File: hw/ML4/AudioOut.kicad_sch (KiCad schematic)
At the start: 24 parts, among them T1 Transformer_1P_1S, U1 LMV324 (Actually LTV9161), U2 LTV-356T, U4 MCP4725xxx-xCH

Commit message: Updates for ML4
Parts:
- R5, R6: value 10k -> 2.2k
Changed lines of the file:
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@@
 			)
 		)
-		(property "Value" "10k"
+		(property "Value" "2.2k"
 			(at 41.91 57.15 0)
 			(effects
@@
 			)
 		)
-		(property "Value" "10k"
+		(property "Value" "2.2k"
 			(at 52.07 62.23 0)
 			(effects

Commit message: Working on JCSC BOM
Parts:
- R1: LCSC (none) -> C4310
- R2: LCSC (none) -> C17530
- R23, R3: LCSC (none) -> C17477
- R24: LCSC (none) -> C17513
- R25: LCSC (none) -> C17633
- R8: value 200 -> 220

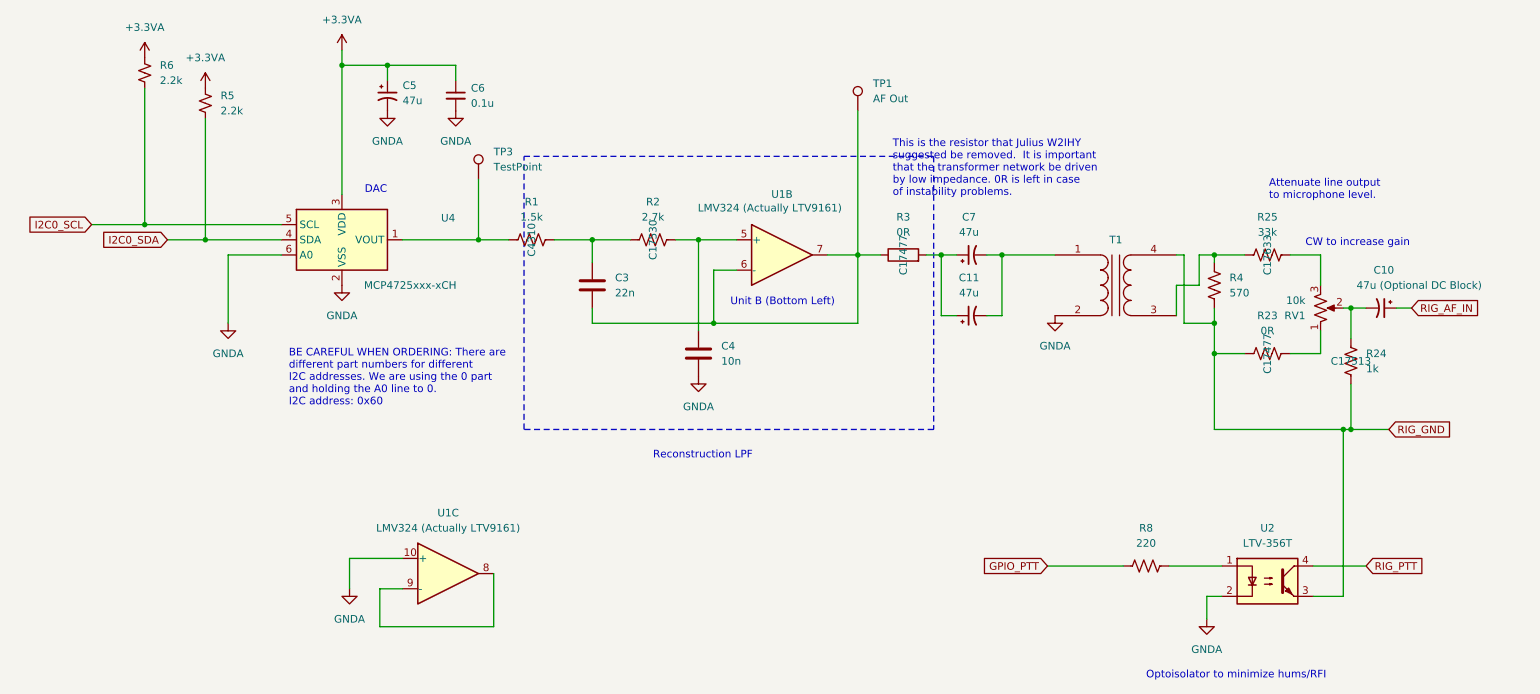
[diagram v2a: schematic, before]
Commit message: Working on adding LCSC part numbers
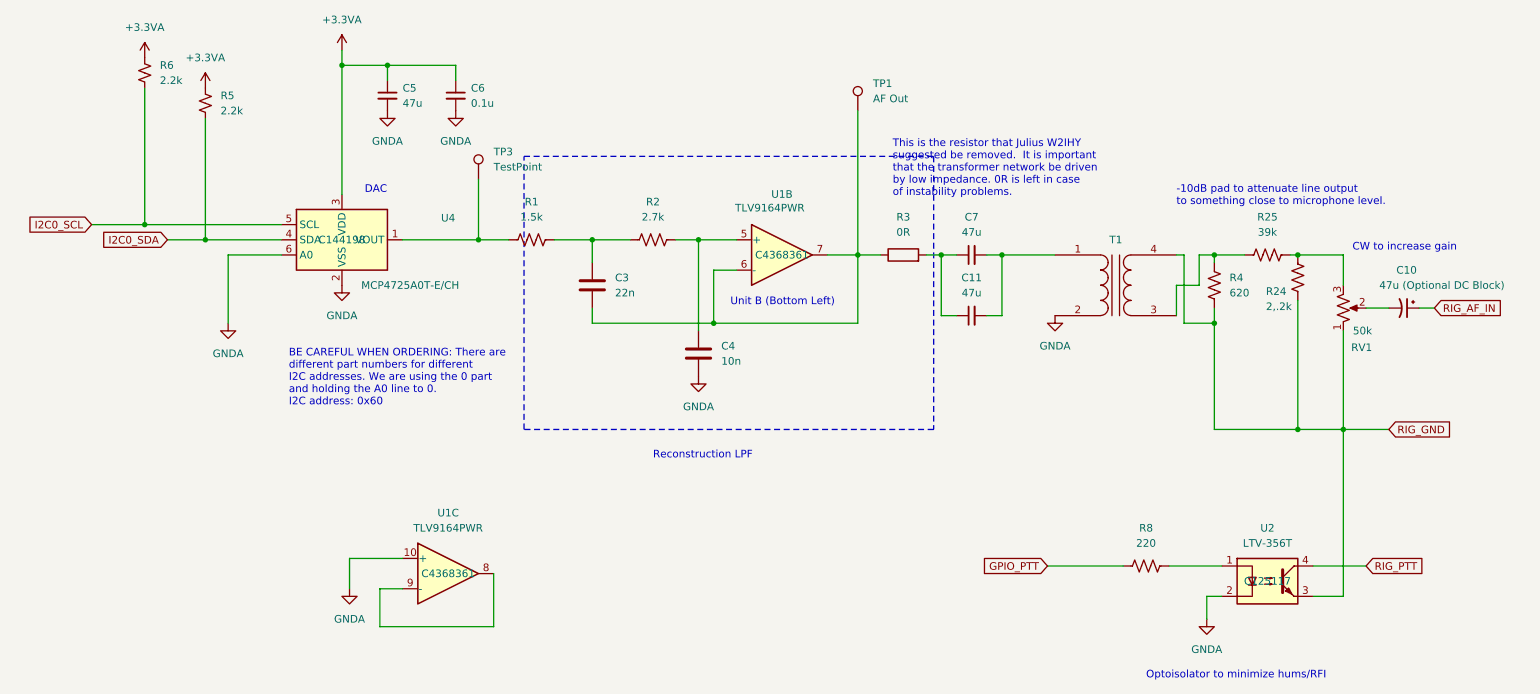
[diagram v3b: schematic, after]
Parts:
- removed C11, C5, C7: 47u, bruce-footprints:CPOL_0805_2012Metric_Pad1.18x1.45mm_HandSolder, symbol Device:C_Polarized_Small_US
- removed R23: 0R, Resistor_SMD:R_0805_2012Metric_Pad1.20x1.40mm_HandSolder, symbol Device:R_US
- added C11, C5, C7: 47u, Capacitor_SMD:C_0805_2012Metric_Pad1.18x1.45mm_HandSolder, symbol Device:C_Small
- C10: LCSC (none) -> C22320
- C3: LCSC (none) -> C1729
- C4: LCSC (none) -> C1710
- C6: LCSC (none) -> C28233
- R24: value 1k -> 2,.2k; LCSC C17513 -> C58595
- R25: value 33k -> 39k; LCSC C17633 -> C58645
- R4: value 570 -> 620; footprint Resistor_SMD:R_0805_2012Metric_Pad1.20x1.40mm_HandSolder -> Resistor_THT:R_Axial_DIN0309_L9.0mm_D3.2mm_P2.54mm_Vertical; LCSC (none) -> C58633
- R5, R6: LCSC (none) -> C17520
- R8: LCSC (none) -> C17557
- RV1: value 10k -> 50k; LCSC (none) -> C81264
- U1: value LMV324 (Actually LTV9161) -> TLV9164PWR; LCSC (none) -> C4368361
- U2: LCSC (none) -> C125117
- U4: value MCP4725xxx-xCH -> MCP4725A0T-E/CH; LCSC (none) -> C144198
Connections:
- net +3.3VA: now also C5.1
- net GNDA: now also C5.2
- net RIG_GND: now also RV1.1
- net at R3.2: now also C11.1, C7.1
- net at T1.1 (AA): now also C11.2, C7.2
- net at C10.2, RV1.2: no longer R24.2
- net at R25.2, RV1.3: now also R24.2
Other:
- note added: "-10dB pad to attenuate line output to something close to microphone level."
- note removed: "Attenuate line output to microphone level."
- moved on the sheet: C10, R24, RV1

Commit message: Working on adding LCSC part numbers
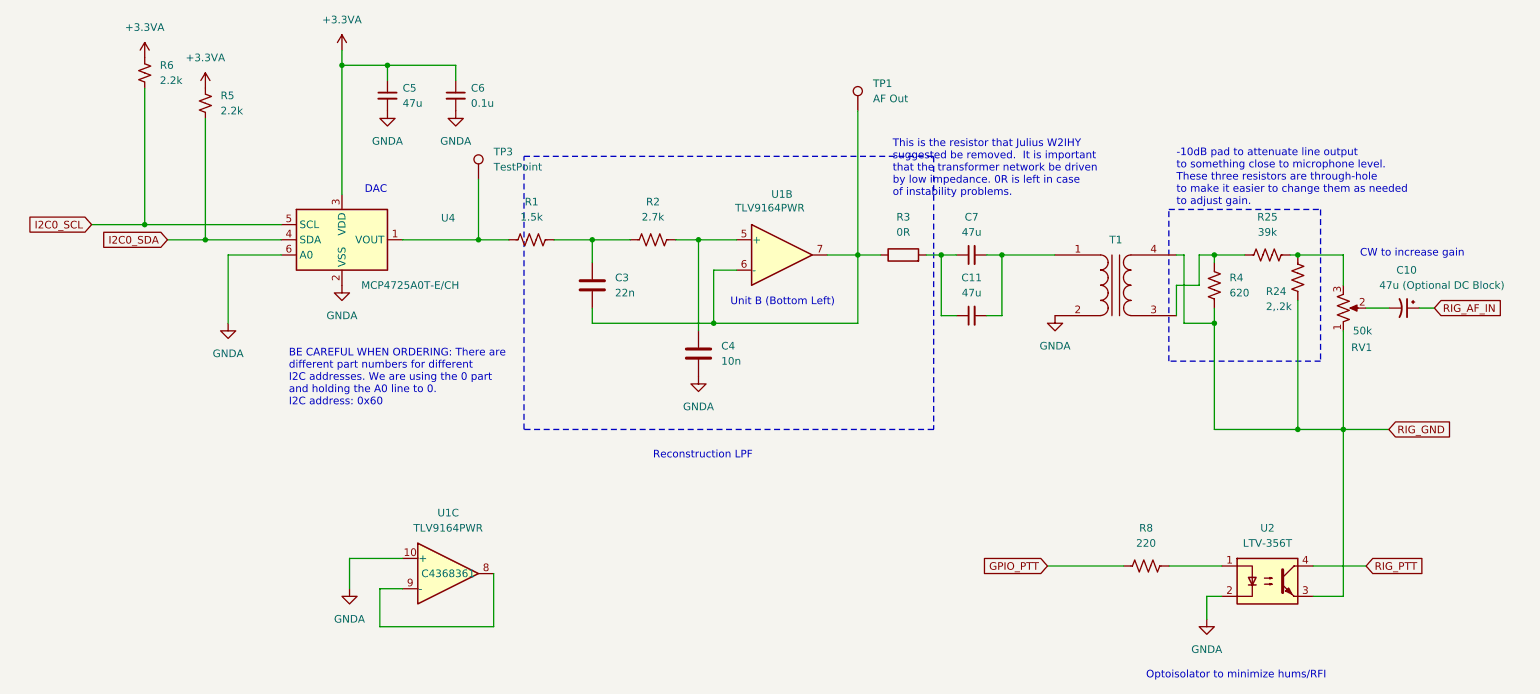
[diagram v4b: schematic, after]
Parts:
- T1: value Transformer_1P_1S -> Transformer_1P_1S 600 Ohm
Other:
- note added: "-10dB pad to attenuate line output to something close to microphone level. These three resistors are through-hole to make it easier to change them as needed to adjust gain."
- note removed: "-10dB pad to attenuate line output to something close to microphone level."
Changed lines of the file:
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@@
 	)
 	(rectangle
+		(start 210.82 78.74)
+		(end 236.22 104.14)
+		(stroke
+			(width 0)
+			(type dot)
+			(color 10 17 255 1)
+		)
+		(fill
+			(type none)
+		)
+	)
+	(rectangle
 		(start 102.87 69.85)
 		(end 171.45 115.57)
@@
 	(text "CW to increase gain"
 		(exclude_from_sim no)
-		(at 241.554 85.852 0)
+		(at 242.824 86.868 0)
 		(effects
 			(font
@@
 		)
 	)
-	(text "-10dB pad to attenuate line output\nto something close to microphone level."
+	(text "-10dB pad to attenuate line output\nto something close to microphone level.\nThese three resistors are through-hole\nto make it easier to change them as needed\nto adjust gain."
 		(exclude_from_sim no)
 		(at 212.09 78.232 0)
@@
 					(size 1.27 1.27)
 				)
+				(hide yes)
 			)
 		)
@@
 					(size 1.27 1.27)
 				)
+				(hide yes)
 			)
 		)
@@
 					(size 1.27 1.27)
 				)
+				(hide yes)
 			)
 		)
@@
 			)
 		)
-		(property "Value" "Transformer_1P_1S"
+		(property "Value" "Transformer_1P_1S 600 Ohm"
 			(at 201.9427 83.82 0)
 			(effects

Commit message: Working on adding LCSC part numbers
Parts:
- T1: BOM Comments (none) -> 600:600 ohm audio transformer (Amazon or AliExpress)
- TP1, TP3: BOM Comments (none) -> No component, PCB test point; now left out of the parts list
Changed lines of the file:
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@@
 		(unit 1)
 		(exclude_from_sim no)
-		(in_bom yes)
+		(in_bom no)
 		(on_board yes)
 		(dnp no)
@@
 					(size 1.27 1.27)
 				)
+			)
+		)
+		(property "BOM Comments" "No component, PCB test point"
+			(at 95.25 73.66 0)
+			(effects
+				(font
+					(size 1.27 1.27)
+				)
+				(hide yes)
+			)
+		)
+		(property "DK" ""
+			(at 95.25 73.66 0)
+			(effects
+				(font
+					(size 1.27 1.27)
+				)
+				(hide yes)
 			)
 		)
@@
 		(unit 1)
 		(exclude_from_sim no)
-		(in_bom yes)
+		(in_bom no)
 		(on_board yes)
 		(dnp no)
@@
 					(size 1.27 1.27)
 				)
+			)
+		)
+		(property "BOM Comments" "No component, PCB test point"
+			(at 158.75 62.23 0)
+			(effects
+				(font
+					(size 1.27 1.27)
+				)
+				(hide yes)
+			)
+		)
+		(property "DK" ""
+			(at 158.75 62.23 0)
+			(effects
+				(font
+					(size 1.27 1.27)
+				)
+				(hide yes)
 			)
 		)
@@
 			)
 		)
+		(property "BOM Comments" "600:600 ohm audio transformer (Amazon or AliExpress)"
+			(at 201.93 91.44 0)
+			(effects
+				(font
+					(size 1.27 1.27)
+				)
+				(hide yes)
+			)
+		)

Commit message: Working on ML4
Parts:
- removed T1: Transformer_1P_1S 600 Ohm, bruce-footprints:CheapAudioTransformer, symbol Device:Transformer_1P_1S
- added TR1: SM-LP-5001, bruce-footprints:TRAN6_SM-LP-5001_BRN, symbol symbol-library-1:SM-LP-5001
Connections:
- net GNDA: now also TR1.3
- net RIG_GND: now also TR1.6
- net at R25.1, R4.1: now also TR1.4
- net at C11.2, C7.2: now also TR1.1
- no-connect marks 0 -> 2
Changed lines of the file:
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@@
 		(color 0 0 0 0)
 	)
+	(no_connect
+		(at 201.93 91.44)
+	)
+	(no_connect
+		(at 191.77 91.44)
+	)
 	(wire
 		(pts
@@
 	(wire
 		(pts
+			(xy 201.93 86.36) (xy 213.36 86.36)
+		)
+		(stroke
+			(width 0)
+			(type default)
+		)
+	)
+	(wire
+		(pts
 			(xy 91.44 54.61) (xy 91.44 57.15)
 		)
@@
 	(wire
 		(pts
-			(xy 212.09 86.36) (xy 213.36 86.36)
-		)
-		(stroke
-			(width 0)
-			(type default)
-		)
-	)
-	(wire
-		(pts
 			(xy 219.71 143.51) (xy 217.17 143.51)
 		)
@@
 	(wire
 		(pts
+			(xy 201.93 96.52) (xy 212.09 96.52)
+		)
+		(stroke
+			(width 0)
+			(type default)
+		)
+	)
+	(wire
+		(pts
 			(xy 134.62 88.9) (xy 134.62 97.79)
 		)
@@
 	)
 	(symbol
+		(lib_id "symbol-library-1:SM-LP-5001")
+		(at 196.85 91.44 0)
+		(unit 1)
+		(exclude_from_sim no)
+		(in_bom yes)
+		(on_board yes)
+		(dnp no)
+		(fields_autoplaced yes)
+		(property "Reference" "TR1"
+			(at 196.85 81.28 0)
+			(effects
+				(font
+					(size 1.27 1.27)
+				)
+			)
+		)
+		(property "Value" "SM-LP-5001"
+			(at 196.85 83.82 0)
+			(effects
+				(font
+					(size 1.27 1.27)
+				)
+			)
+		)
+		(property "Footprint" "bruce-footprints:TRAN6_SM-LP-5001_BRN"
+			(at 196.85 91.44 0)
+			(effects
+				(font
+					(size 1.27 1.27)
+				)
+				(hide yes)
+			)
+		)
+		(property "Datasheet" "https://www.bourns.com/docs/Product-Datasheets/SMLP5001.pdf"
+			(at 196.85 91.44 0)
+			(effects
+				(font
+					(size 1.27 1.27)
+				)
+				(hide yes)
+			)
+		)
+		(property "Description" "Bourns Audio Transformer 1:1 Center Tap"
+			(at 196.85 91.44 0)
+			(effects
+				(font
+					(size 1.27 1.27)
+				)
+				(hide yes)
+			)
+		)
+		(property "LCSC" "C7503474"
+			(at 196.85 91.44 0)
+			(effects
+				(font
+					(size 1.27 1.27)
+				)
+				(hide yes)
+			)
+		)
+		(pin "4"
+		)
+		(pin "1"
+		)
+		(pin "2"
+		)
+		(pin "3"
+		)
+		(pin "6"
+		)
+		(pin "5"
+		)
+		(instances
+			(project ""
+				(path "/5f8f636b-fd0e-498e-8696-0a023acb4c09/5945a24a-f13f-441c-8c0c-8b25494f737c"
+					(reference "TR1")
+					(unit 1)
+				)
+			)
+		)
+	)
+	(symbol
 		(lib_id "Device:R_Small_US")
 		(at 39.37 55.88 0)
@@
 					(unit 1)
 				)
-			)
-		)
-	)
-	(symbol
-		(lib_id "Device:Transformer_1P_1S")
-		(at 201.93 91.44 0)
-		(unit 1)
-		(exclude_from_sim no)
-		(in_bom yes)
-		(on_board yes)
-		(dnp no)
-		(fields_autoplaced yes)
-		(property "Reference" "T1"
-			(at 201.9427 83.82 0)
-			(effects
-				(font
-					(size 1.27 1.27)
-				)
-			)
-		)
-		(property "Value" "Transformer_1P_1S 600 Ohm"
-			(at 201.9427 83.82 0)
-			(effects
-				(font
-					(size 1.27 1.27)
-				)
-				(hide yes)
-			)
-		)
-		(property "Footprint" "bruce-footprints:CheapAudioTransformer"
-			(at 201.93 91.44 0)
-			(effects
-				(font
-					(size 1.27 1.27)
-				)
-				(hide yes)
-			)
-		)
-		(property "Datasheet" "~"
-			(at 201.93 91.44 0)
-			(effects
-				(font
-					(size 1.27 1.27)
-				)
-				(hide yes)
-			)
-		)
-		(property "Description" "Transformer, single primary, single secondary"
-			(at 201.93 91.44 0)
-			(effects
-				(font
-					(size 1.27 1.27)
-				)
-				(hide yes)
-			)
-		)
-		(property "LCSC" ""
-			(at 201.93 91.44 0)
-			(effects
-				(font
-					(size 1.27 1.27)
-				)
-			)
-		)
-		(property "BOM Comments" "600:600 ohm audio transformer (Amazon or AliExpress)"
-			(at 201.93 91.44 0)
-			(effects
-				(font
-					(size 1.27 1.27)
-				)
-				(hide yes)
-			)
-		)
-		(pin "1"
-		)
-		(pin "4"
-		)
-		(pin "3"
-		)
-		(pin "2"
-		)
-		(instances
-			(project "ML4"
-				(path "/5f8f636b-fd0e-498e-8696-0a023acb4c09/5945a24a-f13f-441c-8c0c-8b25494f737c"
-					(reference "T1")
-					(unit 1)
-				)
